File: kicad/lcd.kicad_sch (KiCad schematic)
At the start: 2 parts, among them J501 RVT50HQBNWC00

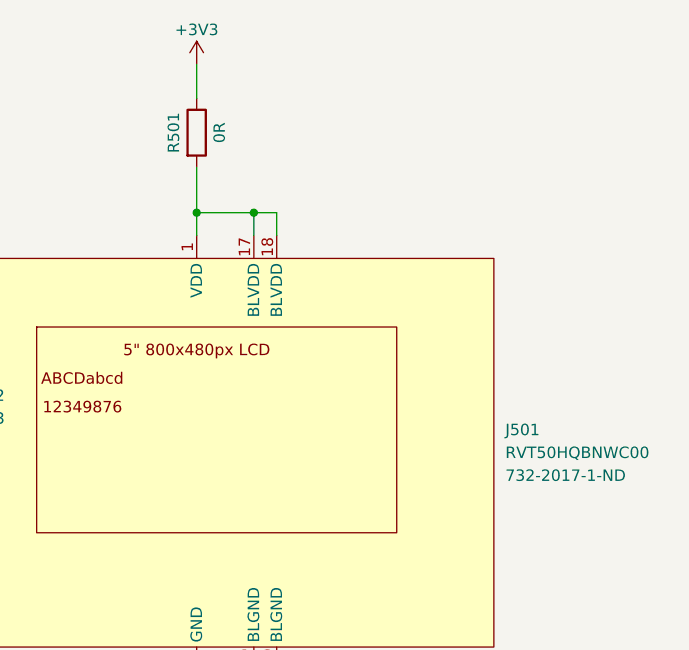
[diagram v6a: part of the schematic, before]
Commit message: add nrf52840 board
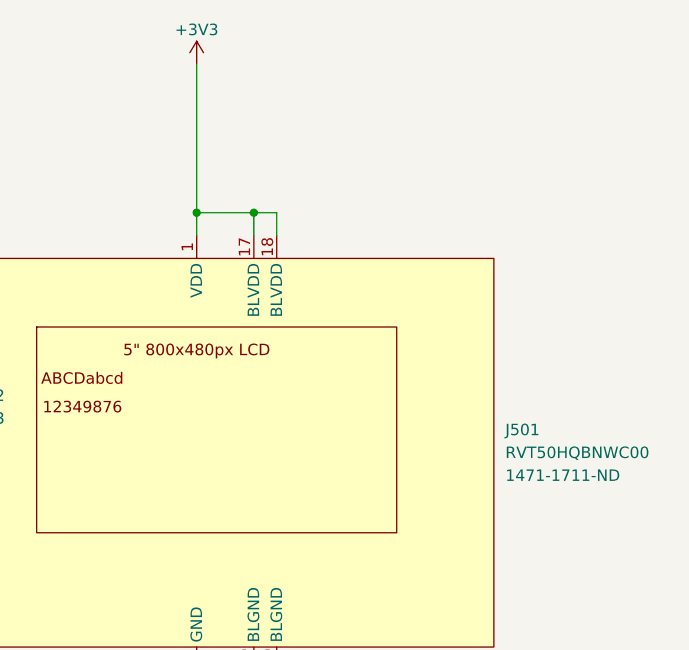
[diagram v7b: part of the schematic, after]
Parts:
- removed R501: 0R, Resistor_SMD:R_0603_1608Metric, symbol Device:R
- J501: Digikey 732-2017-1-ND -> 1471-1711-ND
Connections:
- net +3V3: now also J501.1 (VDD), J501.17 (BLVDD), J501.18 (BLVDD)
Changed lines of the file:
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@@
-    (stroke (width 0) (type default))
-  )
-  (wire (pts (xy 137.16 66.04) (xy 137.16 71.12))
     (stroke (width 0) (type default))
   )
@@
     (stroke (width 0) (type default))
   )
-  (wire (pts (xy 137.16 54.61) (xy 137.16 58.42))
+  (wire (pts (xy 137.16 54.61) (xy 137.16 71.12))
     (stroke (width 0) (type default))
   )
@@
       (effects (font (size 1.27 1.27)) hide)
     )
-    (property "Digikey" "732-2017-1-ND" (at 171.45 100.3299 0)
+    (property "Digikey" "1471-1711-ND" (at 171.45 100.3299 0)
       (effects (font (size 1.27 1.27)) (justify left))
     )
@@
         )
       )
-    )
-  )
-  (symbol (lib_id "Device:R") (at 137.16 62.23 0) (unit 1)
-    (in_bom yes) (on_board yes) (dnp no)
-    (property "Reference" "R501" (at 134.62 62.23 90)
-      (effects (font (size 1.27 1.27)))
-    )
-    (property "Value" "0R" (at 139.7 62.23 90)
-      (effects (font (size 1.27 1.27)))
-    )
-    (property "Footprint" "Resistor_SMD:R_0603_1608Metric" (at 135.382 62.23 90)
-      (effects (font (size 1.27 1.27)) hide)
-    )
-    (property "Datasheet" "~" (at 137.16 62.23 0)
-      (effects (font (size 1.27 1.27)) hide)
-    )
-    (property "Digikey" "541-0.0SBCT-ND" (at 137.16 62.23 0)
-      (effects (font (size 1.27 1.27)) hide)
-    )
-    (pin "1")
-    (pin "2")
-    (instances
-      (project "firewaterburn"
-        (path "/e63e39d7-6ac0-4ffd-8aa3-1841a4541b55/5d28ac6a-038b-41fa-a41c-77399bf887bc"
-          (reference "R501") (unit 1)
-        )
-      )

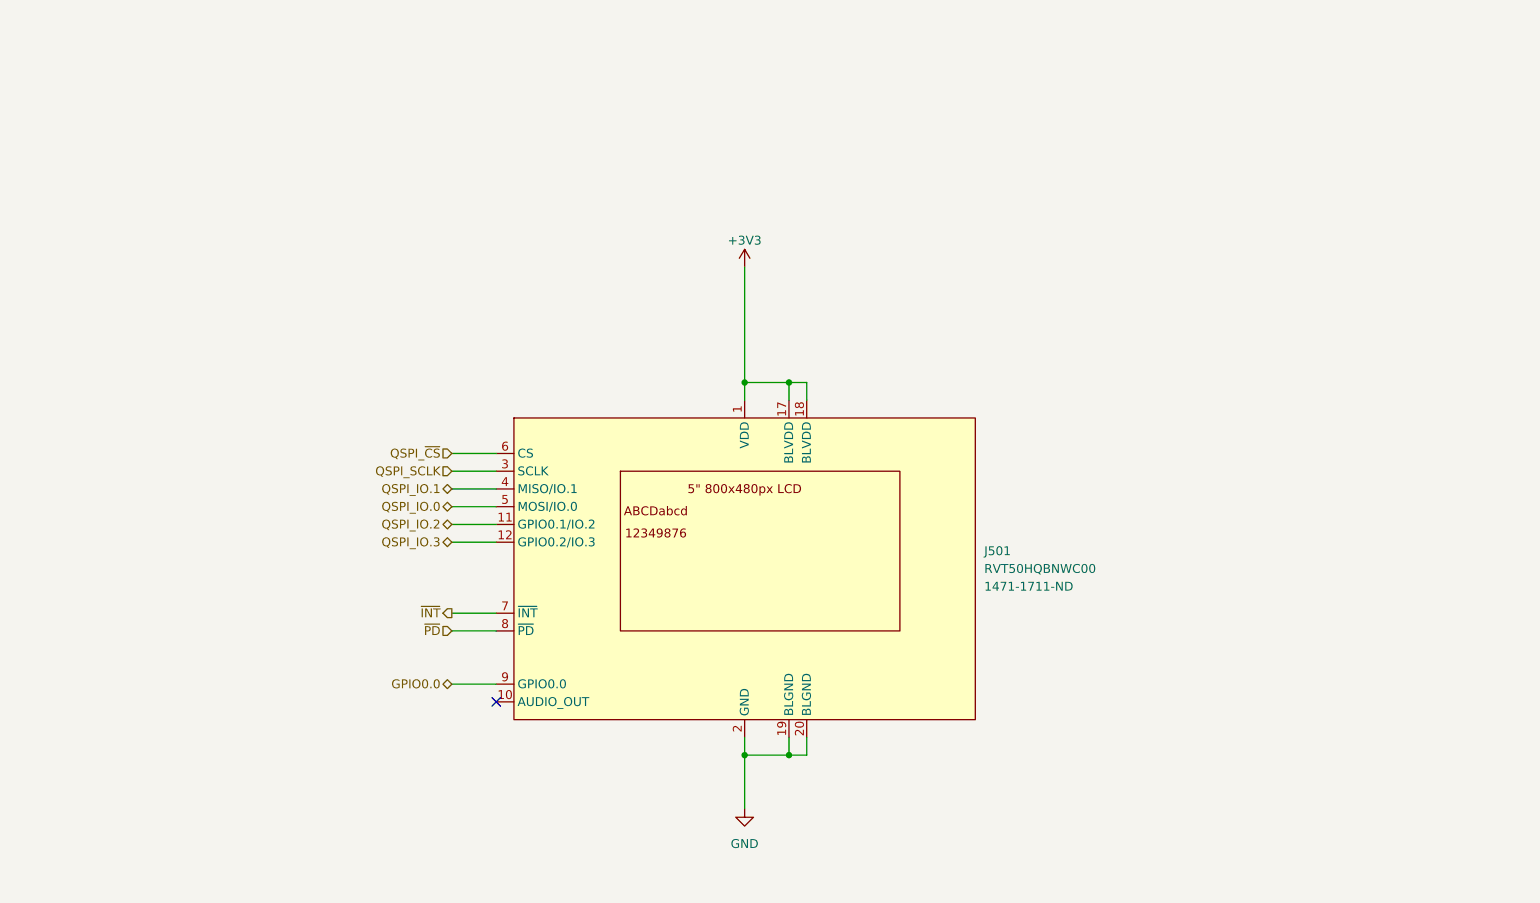
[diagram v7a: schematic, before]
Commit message: rework board
add nrf 7002
add oled display
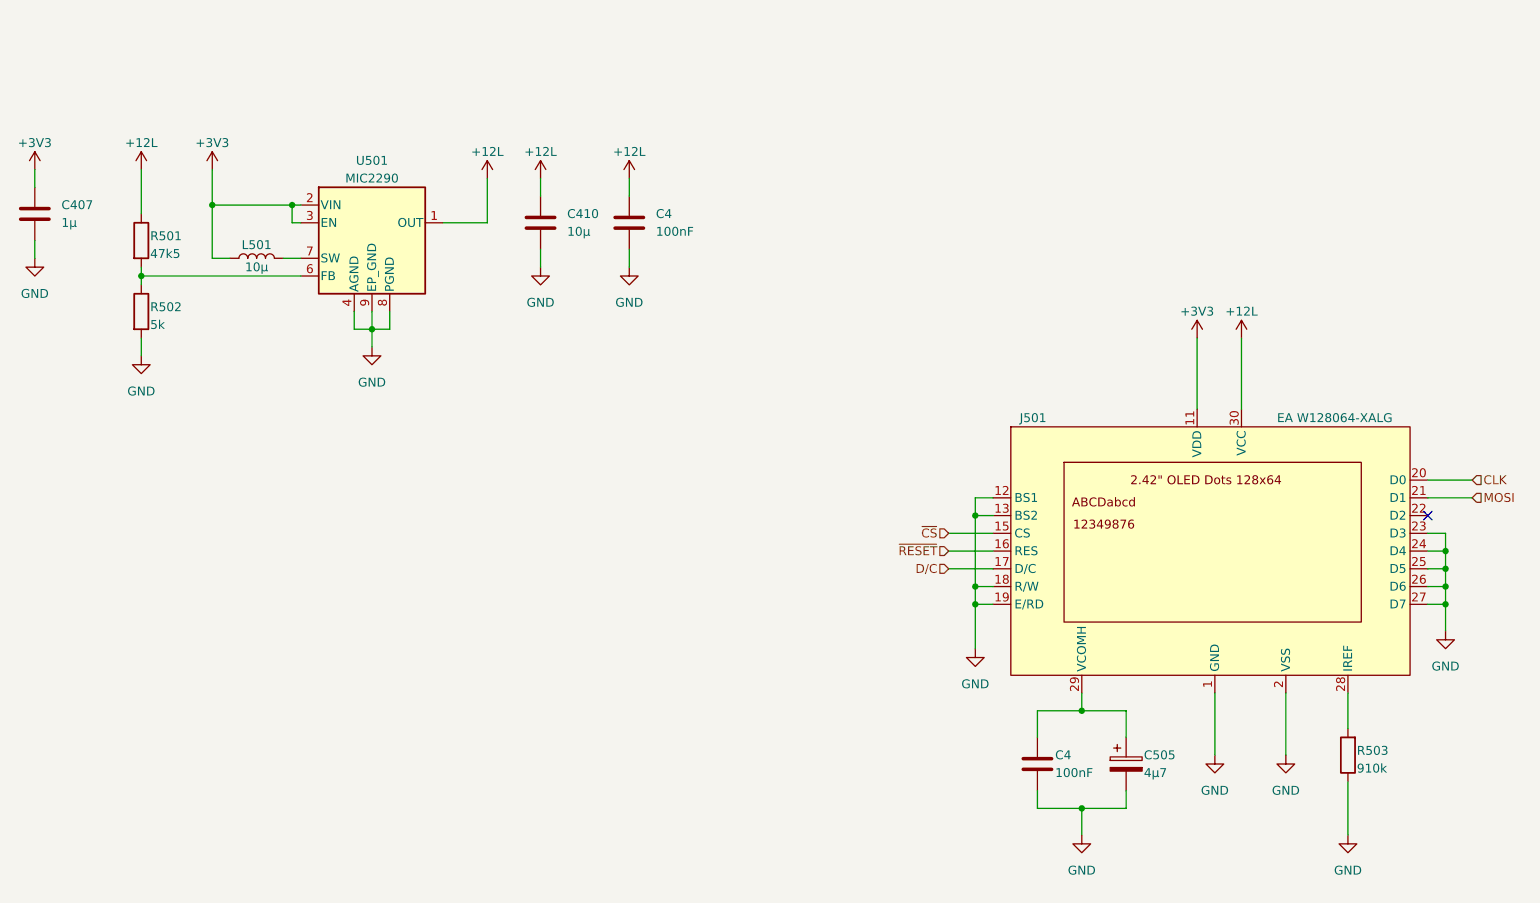
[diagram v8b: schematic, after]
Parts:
- removed J501: RVT50HQBNWC00, mylib_connector:FPC_BOTTOM_20POS_Würth_68712014522, symbol mylib_ic:RVT50HQBNWC00
- added C4: 100nF, Capacitor_SMD:C_0603_1608Metric, symbol Device:C
- added C4: 100nF, Capacitor_SMD:C_0402_1005Metric, symbol Device:C
- added C407: 1µ, Capacitor_SMD:C_0402_1005Metric, symbol Device:C
- added C410: 10µ, Capacitor_SMD:C_0402_1005Metric, symbol Device:C
- added C505: 4µ7, Capacitor_Tantalum_SMD:CP_EIA-2012-15_AVX-P, symbol Device:C_Polarized
- added J501: EA W128064-XALG, mylib_connector:SFV31R-4STE1HLF, symbol mylib_ic:EA W128064-XALG
- added L501: 10µ, Inductor_SMD:L_Wuerth_MAPI-2510, symbol Device:L
- added R501: 47k5, Resistor_SMD:R_0402_1005Metric, symbol Device:R
- added R502: 5k, Resistor_SMD:R_0402_1005Metric, symbol Device:R
- added R503: 910k, Resistor_SMD:R_0603_1608Metric, symbol Device:R
- added U501: MIC2290, mylib_ic:Micrel_MLF-8-1EP_2x2mm_P0.5mm_EP0.8x1.3mm_ThermalVias, symbol Regulator_Switching:MIC2290
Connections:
- net +3V3: now also C407.1, J501.11 (VDD), L501.1, U501.2 (VIN), U501.3 (EN)
- net GND: now also C4.2, C4.2, C407.2, C410.2, C505.2, J501.1 (GND), J501.12 (BS1), J501.13 (BS2), J501.18 (R/W), J501.19 (E/RD), J501.2 (VSS), J501.23 (D3), J501.24 (D4), J501.25 (D5), J501.26 (D6), J501.27 (D7), J501.31 (GND), R502.2, R503.1, U501.4 (AGND), U501.8 (PGND), U501.9 (EP_GND)
- new net: R501.2, R502.1, U501.6 (FB)
- new net: L501.2, U501.7 (SW)
- new net: C4.1, C505.1, J501.29 (VCOMH)
- new net: J501.28 (IREF), R503.2
- new net: J501.10, J501.14, J501.3, J501.4, J501.5, J501.6, J501.7, J501.8, J501.9
- new net +12L: C4.1, C410.1, J501.30 (VCC), R501.1, U501.1 (OUT)
- new net CLK: J501.20 (D0)
- new net D/C: J501.17 (D/C)
- new net MOSI: J501.21 (D1)
- new net ~{CS}: J501.15 (CS)
- new net ~{RESET}: J501.16 (RES)
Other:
- title: (none) -> Firewaterburn
